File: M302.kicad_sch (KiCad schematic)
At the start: 28 parts, among them J1 I2C-SHT3x, J2 I2C-ThmCp, J3 I2C-3, J4 I2C-4, J5 I2C-D400, J6 W5500, J7 IM920, J8 PWR+5V, J9 ANALOG-IN, P1 Power, P2 Analog, P3 Digital, P4 Digital, P5 CONN_01X01, P6 CONN_01X01, P7 CONN_01X01, P8 CONN_01X01, SW1 CPU, SW2 D400, SW3 IM920, U1 SFE-BOB-12009

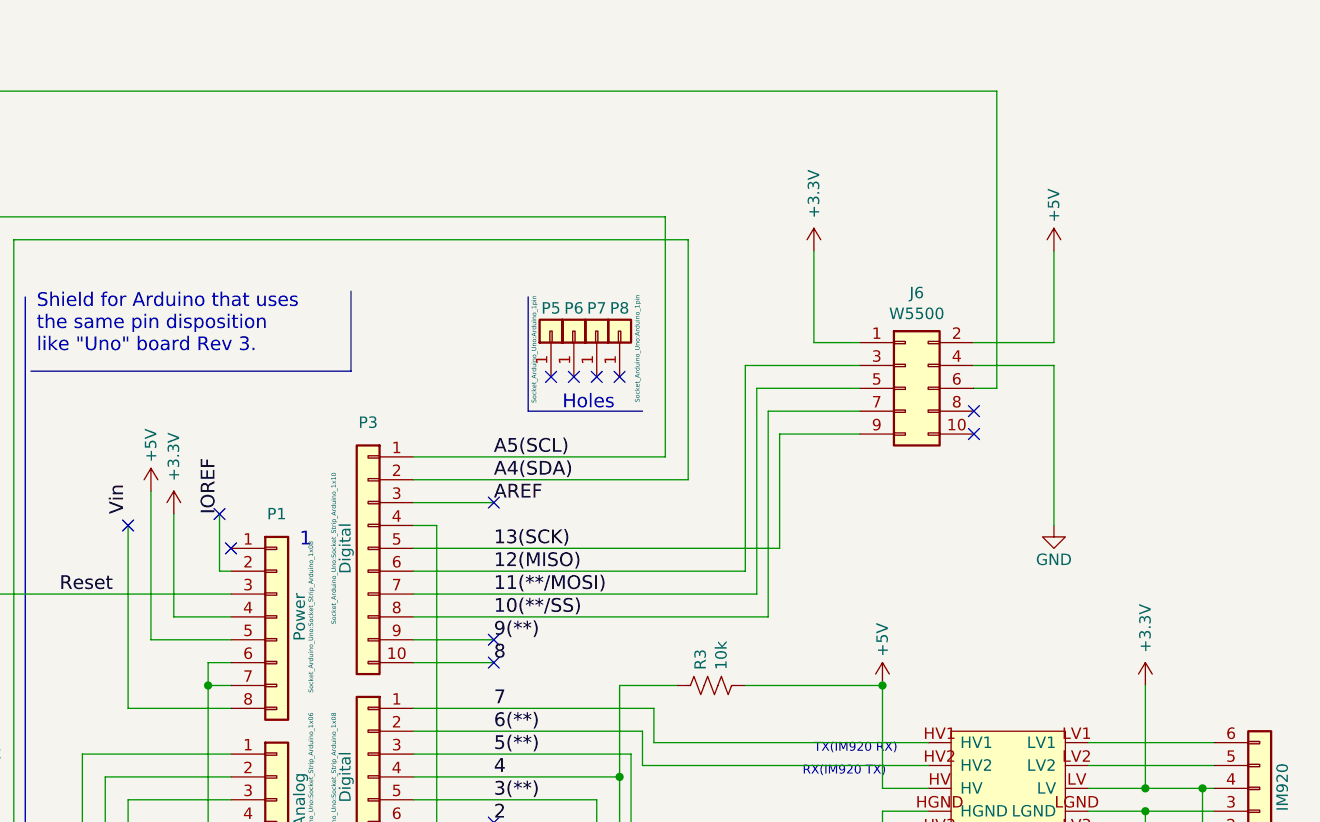
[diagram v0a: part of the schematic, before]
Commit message: KiCAD 8.0
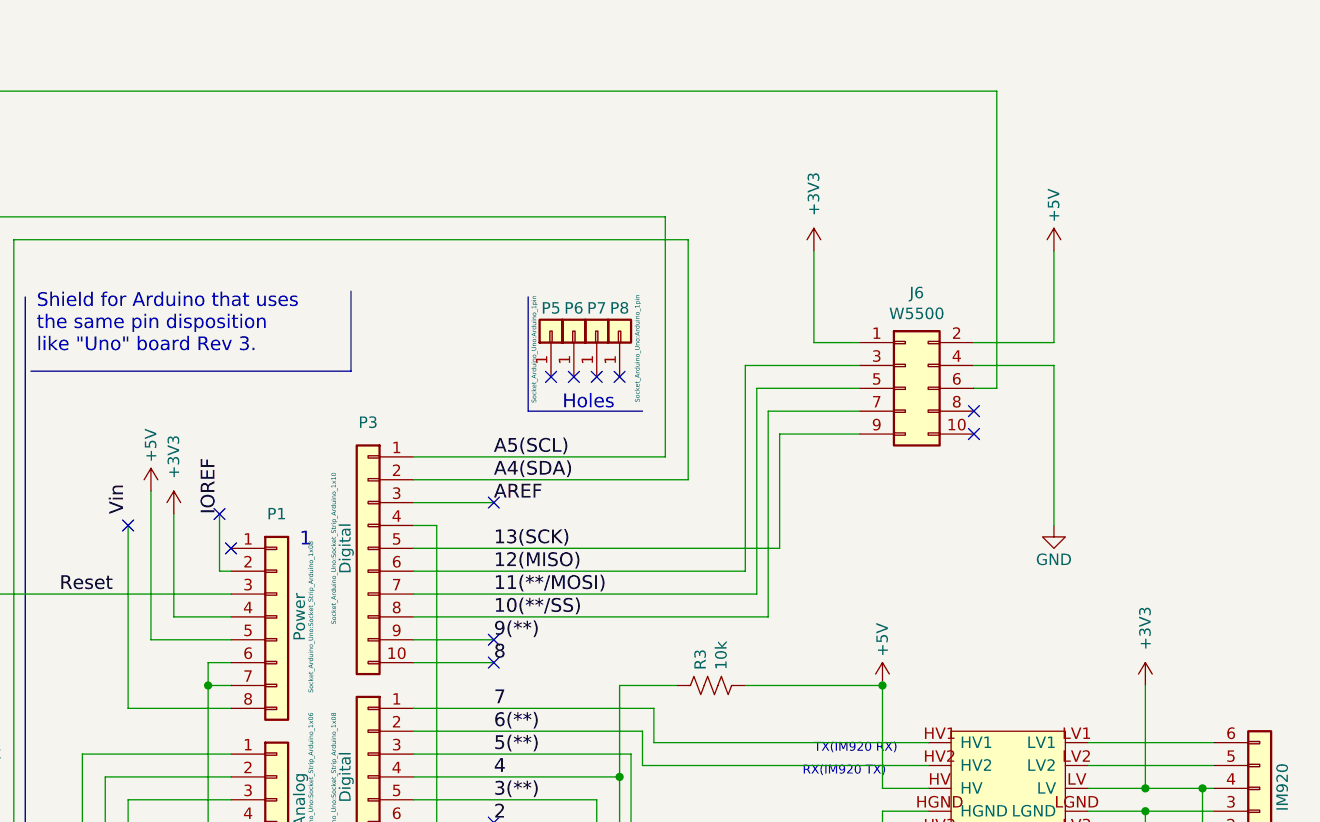
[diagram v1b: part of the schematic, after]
